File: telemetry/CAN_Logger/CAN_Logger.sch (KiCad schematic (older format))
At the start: 53 parts, among them J1 CONN_02X03, J2 SD_socket, U1 MCP2561-E_SN, U101 TPS560430YF, U2 ATMEGA16M1, U3 LM3480, U4 TXB0104, U5 R_500, U6 R_500, U7 R_500, Y1 Crystal_SMD

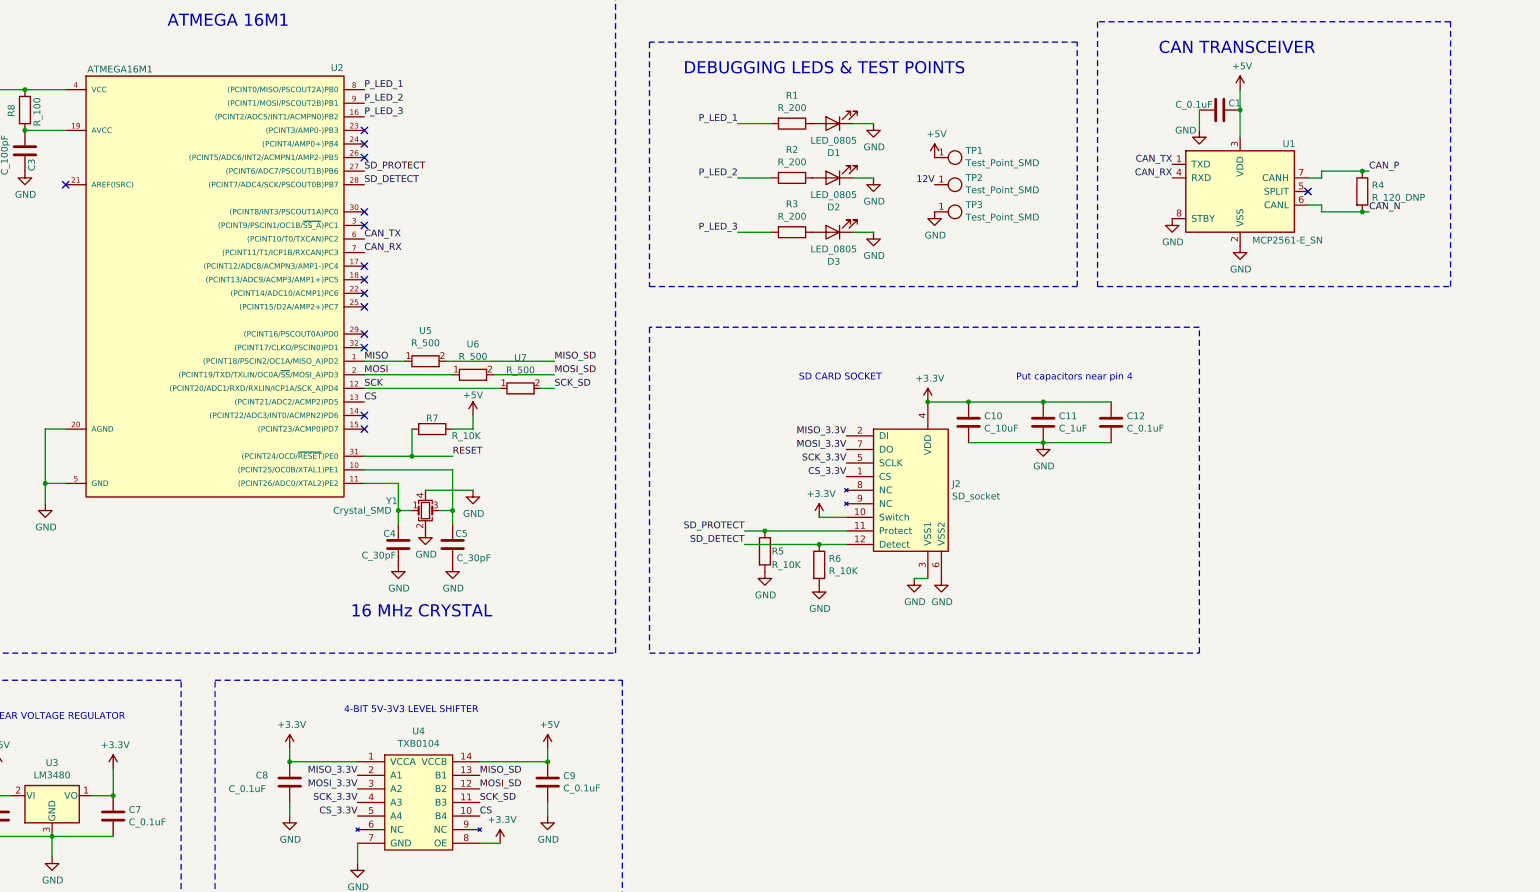
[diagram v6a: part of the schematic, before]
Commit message: Small changes: 3.3V->3V3, added test points to Debug LEDS, etc.
Following recommendations given by Wesley, pg. 2 of this file:
https://drive.google.com/file/d/12oTchTOrF_66K-js-7AgllKoxS_4IslO/view.
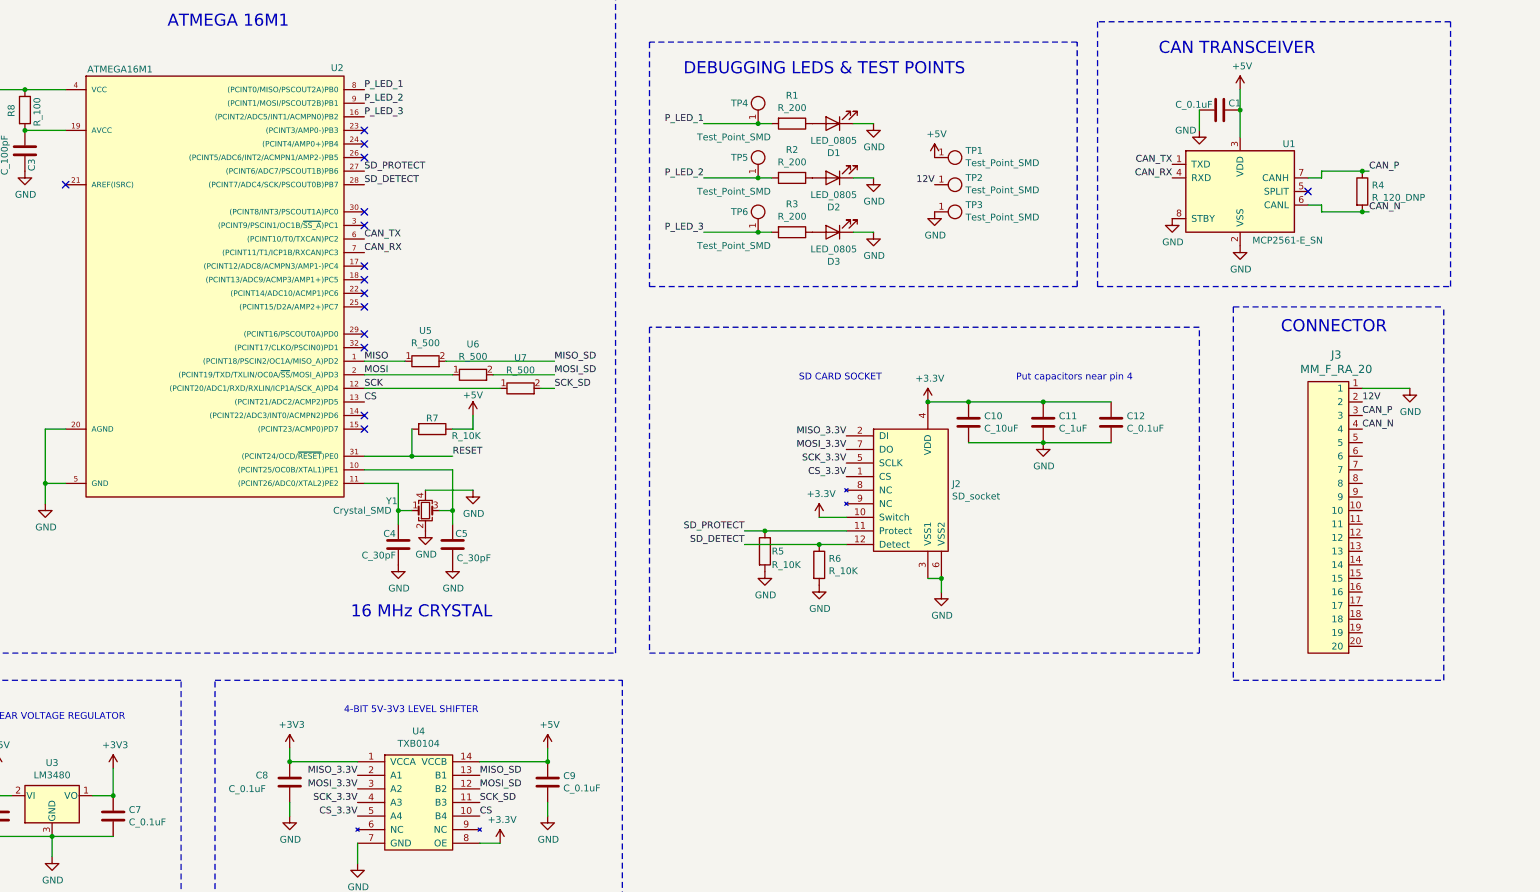
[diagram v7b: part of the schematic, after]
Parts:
- added J3: MM_F_RA_20, footprints:micromatch_female_ra_20, symbol formula:MM_F_RA_20
- added TP4, TP5, TP6: Test_Point_SMD, footprints:Test_Point_SMD, symbol formula:Test_Point_SMD
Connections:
- net 12V: now also J3.2
- net CAN_N: now also J3.4
- net CAN_P: now also J3.3
- net GND: now also J3.1
- net P_LED_1: now also TP4.1
- net P_LED_2: now also TP5.1
- net P_LED_3: now also TP6.1
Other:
- note added: "CONNECTOR"

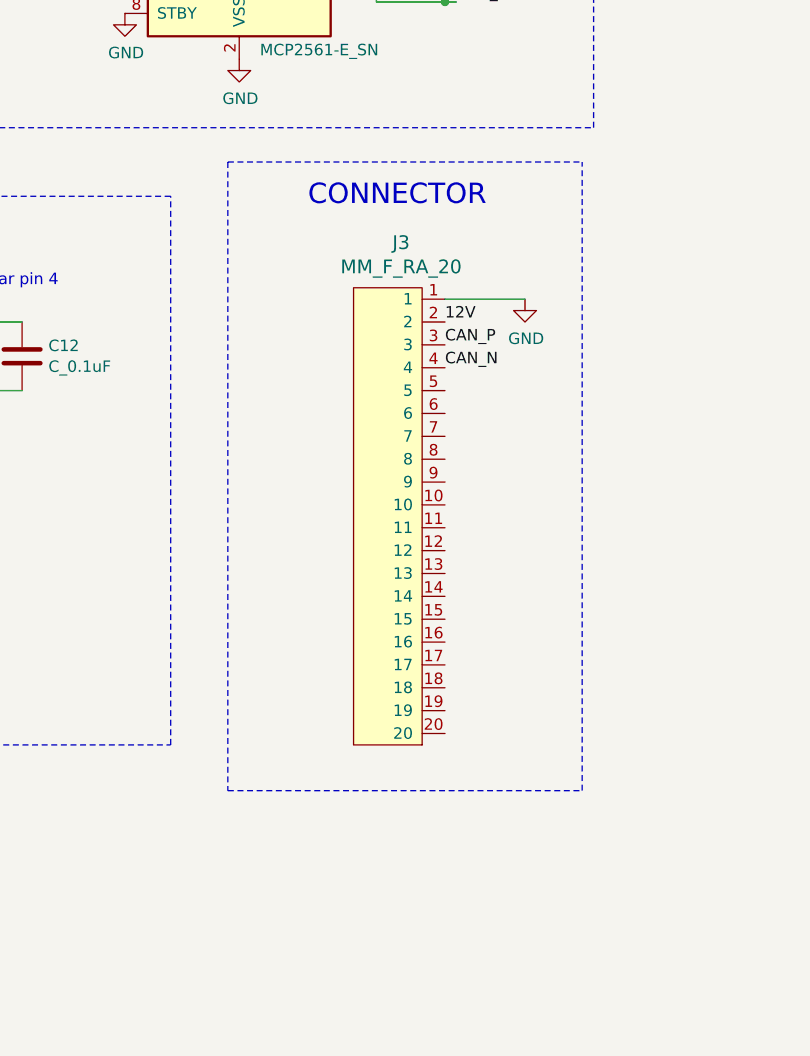
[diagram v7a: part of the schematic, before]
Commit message: PCB Layout: grouped together functional blocks, added GND to connector
Grouped functional blocks together by component in PCB layout, connected connector to ground. Layout is currently off board.
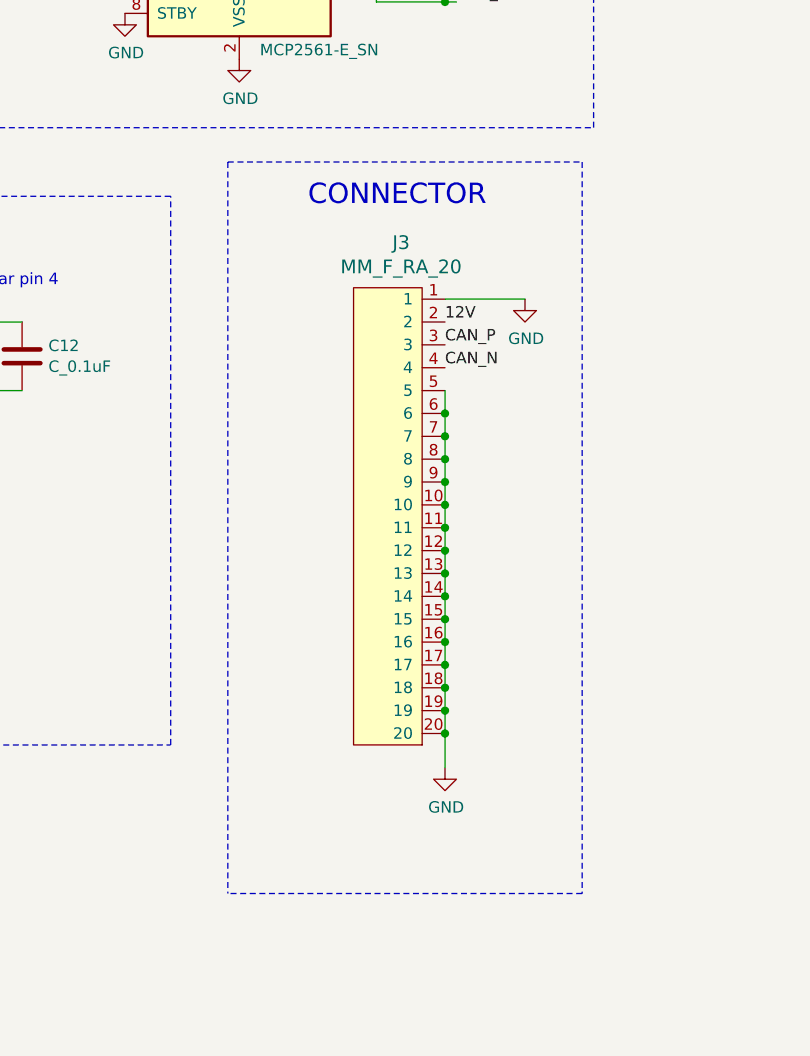
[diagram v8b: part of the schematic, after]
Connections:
- net GND: now also J3.10, J3.11, J3.12, J3.13, J3.14, J3.15, J3.16, J3.17, J3.18, J3.19, J3.20, J3.5, J3.6, J3.7, J3.8, J3.9
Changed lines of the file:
@@
 	6950 2150 7050 2150
 $Comp
-L power:+3V3 #PWR?
+L power:+3V3 #PWR0109
 U 1 1 60360B9B
 P 2200 6500
-F 0 "#PWR?" H 2200 6350 50  0001 C CNN
+F 0 "#PWR0109" H 2200 6350 50  0001 C CNN
 F 1 "+3V3" H 2215 6673 50  0000 C CNN
 F 2 "" H 2200 6500 50  0001 C CNN
@@
 Connection ~ 2200 6700
 $Comp
-L power:+3V3 #PWR?
+L power:+3V3 #PWR0111
 U 1 1 60373CBA
 P 3500 6350
-F 0 "#PWR?" H 3500 6200 50  0001 C CNN
+F 0 "#PWR0111" H 3500 6200 50  0001 C CNN
 F 1 "+3V3" H 3515 6523 50  0000 C CNN
 F 2 "" H 3500 6350 50  0001 C CNN
@@
 $EndComp
 Wire Notes Line
-	10450 3100 10450 5850
+	10450 3100 12000 3100
+$Comp
+L power:GND #PWR?
+U 1 1 60394B7B
+P 11400 5750
+F 0 "#PWR?" H 11400 5500 50  0001 C CNN
+F 1 "GND" H 11405 5577 50  0000 C CNN
+F 2 "" H 11400 5750 50  0001 C CNN
+F 3 "" H 11400 5750 50  0001 C CNN
+	1    11400 5750
+	1    0    0    -1
+$EndComp
 Wire Notes Line
-	10450 5850 12000 5850
+	12000 6300 10450 6300
 Wire Notes Line
-	12000 5850 12000 3100
+	10450 3100 10450 6300
 Wire Notes Line
-	10450 3100 12000 3100
+	12000 3100 12000 6300
+Wire Wire Line
+	11400 4200 11400 4300
+Connection ~ 11400 4300
+Wire Wire Line
+	11400 4300 11400 4400
+Connection ~ 11400 4400
+Wire Wire Line
+	11400 4400 11400 4500
+Connection ~ 11400 4500
+Wire Wire Line
+	11400 4500 11400 4600
+Connection ~ 11400 4600
+Wire Wire Line
+	11400 4600 11400 4700
+Connection ~ 11400 4700
+Wire Wire Line
+	11400 4700 11400 4800
+Connection ~ 11400 4800
+Wire Wire Line
+	11400 4800 11400 4900
+Connection ~ 11400 4900
+Wire Wire Line
+	11400 4900 11400 5000
+Connection ~ 11400 5000
+Wire Wire Line
+	11400 5000 11400 5100
+Connection ~ 11400 5100
+Wire Wire Line
+	11400 5100 11400 5200
+Connection ~ 11400 5200
+Wire Wire Line
+	11400 5200 11400 5300
+Connection ~ 11400 5300
+Wire Wire Line
+	11400 5300 11400 5400
+Connection ~ 11400 5400
+Wire Wire Line
+	11400 5400 11400 5500
+Connection ~ 11400 5500
+Wire Wire Line
+	11400 5500 11400 5600
+Connection ~ 11400 5600
+Wire Wire Line
+	11400 5600 11400 5750
+Wire Wire Line
+	11400 4200 11400 4100
+Connection ~ 11400 4200
 $EndSCHEMATC
